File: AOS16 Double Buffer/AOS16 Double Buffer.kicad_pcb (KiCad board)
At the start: 4 copper layers, 47 x 72 mm, 45 parts, among them IC1 IS61WV3216BLL-12TLI, IC2 SN74LVC16245ADGVR, IC3 SN74LVC16245ADGVR, IC4 SN74LVC16245ADGVR, IC5 SN74LVC16245ADGVR, J1 Conn_01x02_Pin, J2 Conn_02x08_Top_Bottom, J3 Conn_02x08_Top_Bottom, J4 Conn_02x08_Top_Bottom, J5 Conn_02x08_Top_Bottom, J6 Conn_01x07_Pin, U1 74AHC1G08, U2 74AHC1G08, U3 74AHC1G32, U4 74AHC1G32, U5 74AHC1G04, U6 74AHC1G04, U7 74LS157

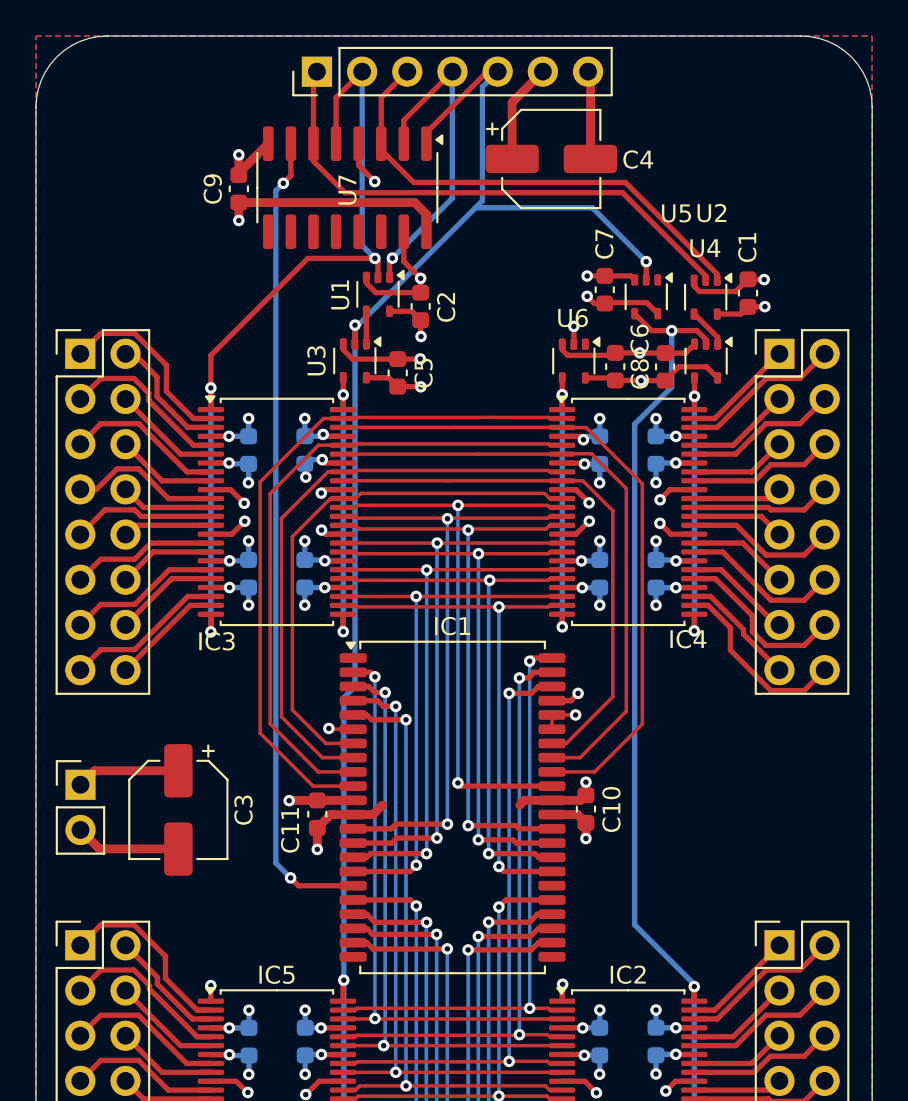
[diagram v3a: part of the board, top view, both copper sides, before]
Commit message: Finalized double buffer
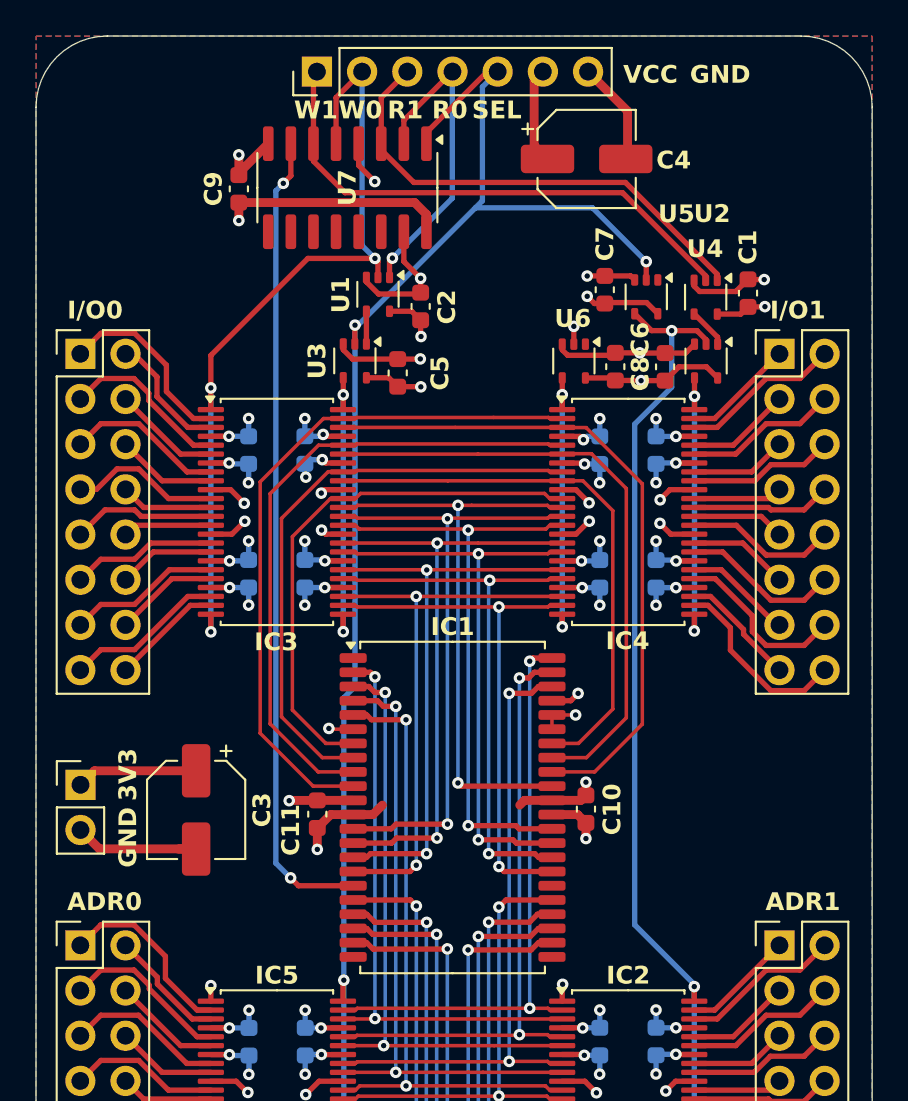
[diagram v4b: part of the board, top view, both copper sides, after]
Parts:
- moved C4 1.99 mm to (55.0, 56.9)
- moved C3 1.00 mm to (33.0, 93.5)
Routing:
- net GND: track 142.1 -> 144.9 mm
- net +3.3V: track 65.5 -> 66.5 mm
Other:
- board text added: "3V3"
- board text added: "ADR0"
- board text added: "ADR1"
- board text added: "GND"
- board text added: "I/O0"
- board text added: "I/O1"
- board text added: "R0"
- board text added: "R1"
- board text added: "SEL"
- board text added: "VCC"
- board text added: "W0"
- board text added: "W1"

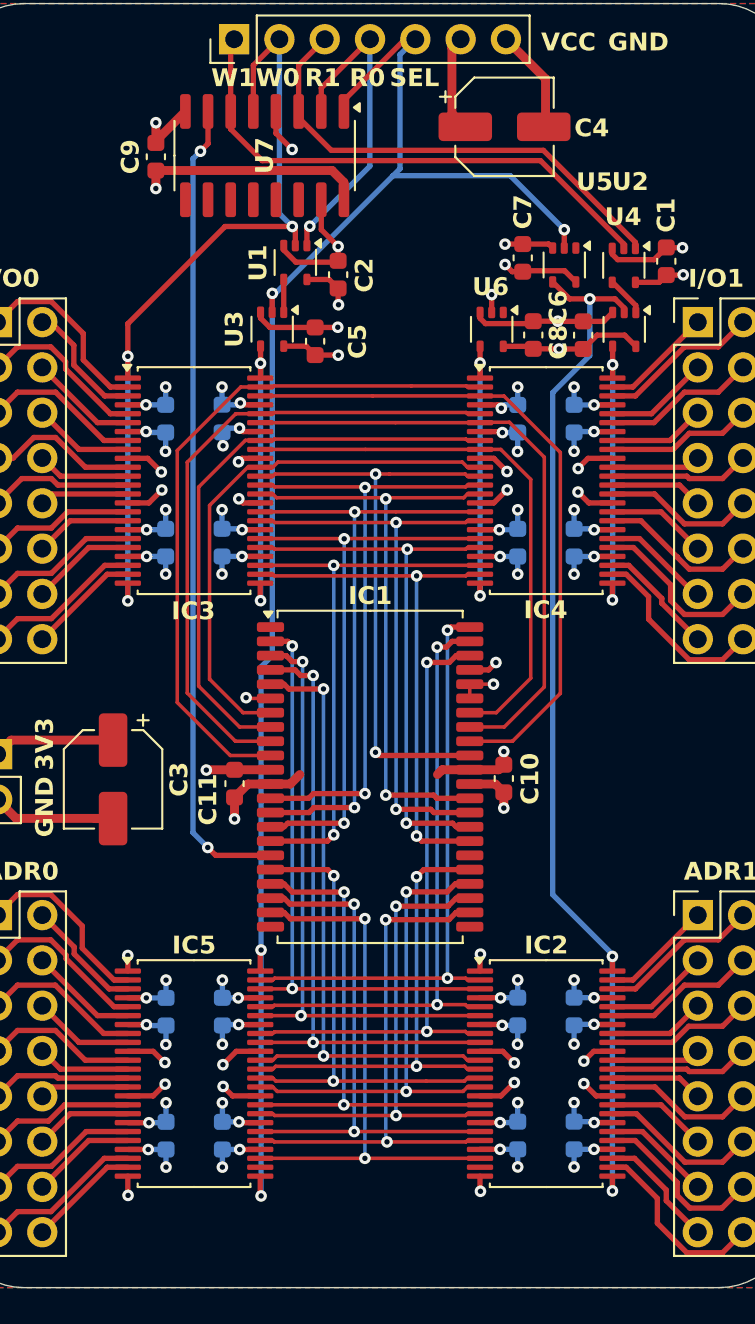
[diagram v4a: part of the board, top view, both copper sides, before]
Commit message: Double Buffer Revision
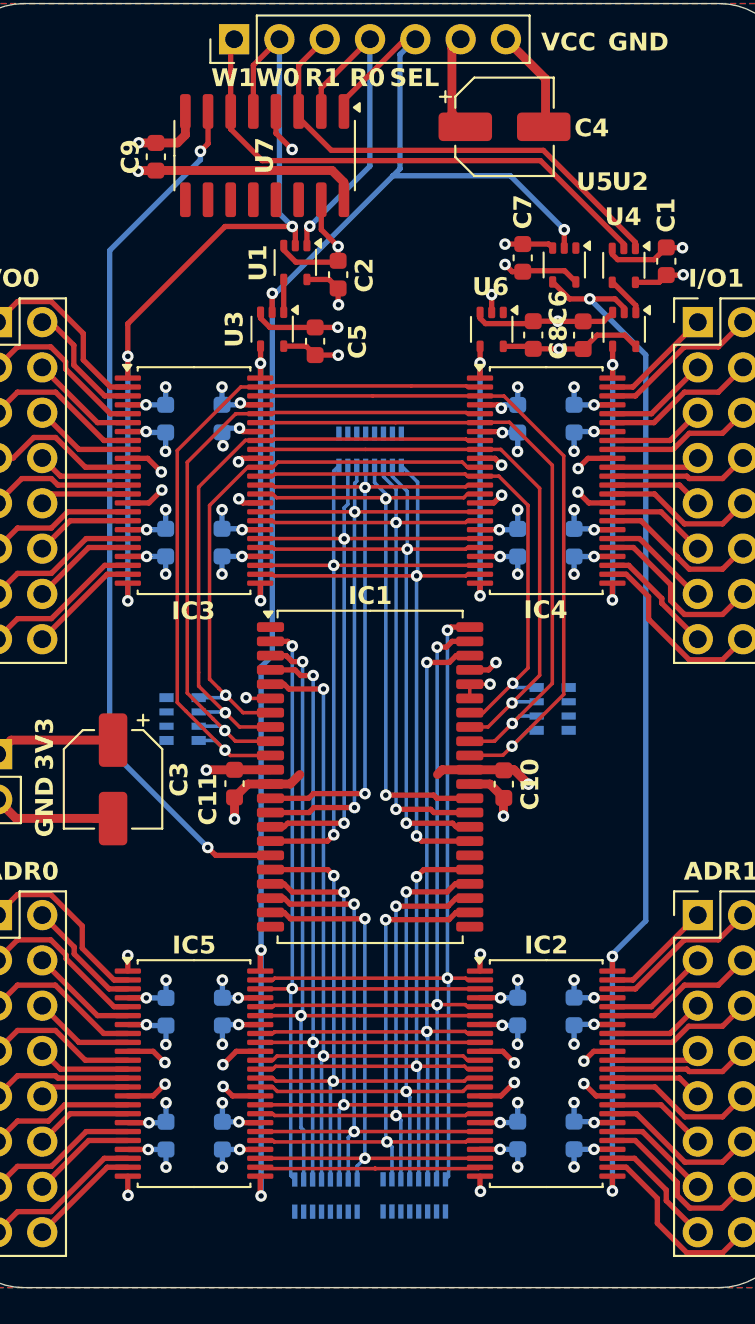
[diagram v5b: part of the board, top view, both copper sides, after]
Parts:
- added RN1: R_Pack08, Resistor_SMD:R_Array_Convex_8x0602, B.Cu at (44.9, 116.8)
- added RN2: R_Pack08, Resistor_SMD:R_Array_Convex_8x0602, B.Cu at (49.9, 116.8)
- added RN3: R_Pack04, Resistor_SMD:R_Array_Convex_4x0603, B.Cu at (57.6, 89.5)
- added RN4: R_Pack04, Resistor_SMD:R_Array_Convex_4x0603, B.Cu at (36.9, 90.1)
- added RN5: R_Pack08, Resistor_SMD:R_Array_Convex_8x0602, B.Cu at (47.4, 75.0)
- moved C10 0.31 mm to (54.9, 93.8)
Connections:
- net /ram/INA0 renamed /pull_resistor/IN0
- net /ram/INA1 renamed /pull_resistor/IN1
- net /ram/INA10 renamed /pull_resistor/IN10
- net /ram/INA11 renamed /pull_resistor/IN11
- net /ram/INA12 renamed /pull_resistor/IN12
- net /ram/INA13 renamed /pull_resistor/IN13
- net /ram/INA14 renamed /pull_resistor/IN14
- net /ram/INA2 renamed /pull_resistor/IN2
- net /ram/INA3 renamed /pull_resistor/IN3
- net /ram/INA4 renamed /pull_resistor/IN4
- net /ram/INA5 renamed /pull_resistor/IN5
- net /ram/INA6 renamed /pull_resistor/IN6
- net /ram/INA7 renamed /pull_resistor/IN7
- net /ram/INA8 renamed /pull_resistor/IN8
- net /ram/INA9 renamed /pull_resistor/IN9
- IC1 pad 35: /ram/OUT7 -> /ram/OUT1
- IC1 pad 36: /ram/OUT1 -> /ram/OUT3
- IC1 pad 37: /ram/OUT3 -> /ram/OUT5
- IC1 pad 38: /ram/OUT5 -> /ram/OUT7
- IC2 pad 23: /word_buffer1/B15 -> /pull_resistor/IN15
- IC5 pad 26: /word_buffer/A15 -> /pull_resistor/IN15
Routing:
- net /pull_resistor/IN15: track 0.00 -> 12.4 mm
- net /pull_resistor/IN0: track 33.2 -> 44.6 mm
- net /pull_resistor/IN1: track 32.9 -> 43.7 mm
- net /pull_resistor/IN2: track 34.4 -> 44.2 mm
- net /pull_resistor/IN3: track 34.2 -> 43.4 mm
- net /pull_resistor/IN4: track 35.7 -> 44.0 mm
- net /pull_resistor/IN5: track 35.6 -> 43.3 mm
- net /pull_resistor/IN6: track 36.2 -> 43.2 mm
- net /ram/OUT15: track 30.2 -> 36.8 mm
- net /pull_resistor/IN7: track 26.2 -> 32.6 mm
- net /ram/OUT14: track 31.1 -> 36.8 mm
- net /pull_resistor/IN8: track 27.7 -> 33.3 mm
- net /ram/OUT13: track 31.4 -> 36.5 mm
- net /pull_resistor/IN9: track 27.5 -> 32.5 mm
- net /pull_resistor/IN10: track 28.6 -> 32.9 mm
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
